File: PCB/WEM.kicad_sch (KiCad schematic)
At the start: 79 parts, among them J1 USB_C_Receptacle_USB2.0_14P, J2 MCU flashing pins, J3 Extensions' connectors, J4 Battery, J5 Reset, J6 Battery jumper, SW1 Kailh Mouse Scroll Wheel Enco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, SW2 LMB, SW3 MMB, SW4 RMB, SW5 FORWARD, SW6 BACK, SW7 SMMB, SW8 ON/OFF, U1 nRF52840, U2 MCP73871-2CC, U3 PAW3395DM-T6QU, U4 MCP1801T-3302I_OT, U5 LT1761ES5-2-TRMPBF, X1 32MHz

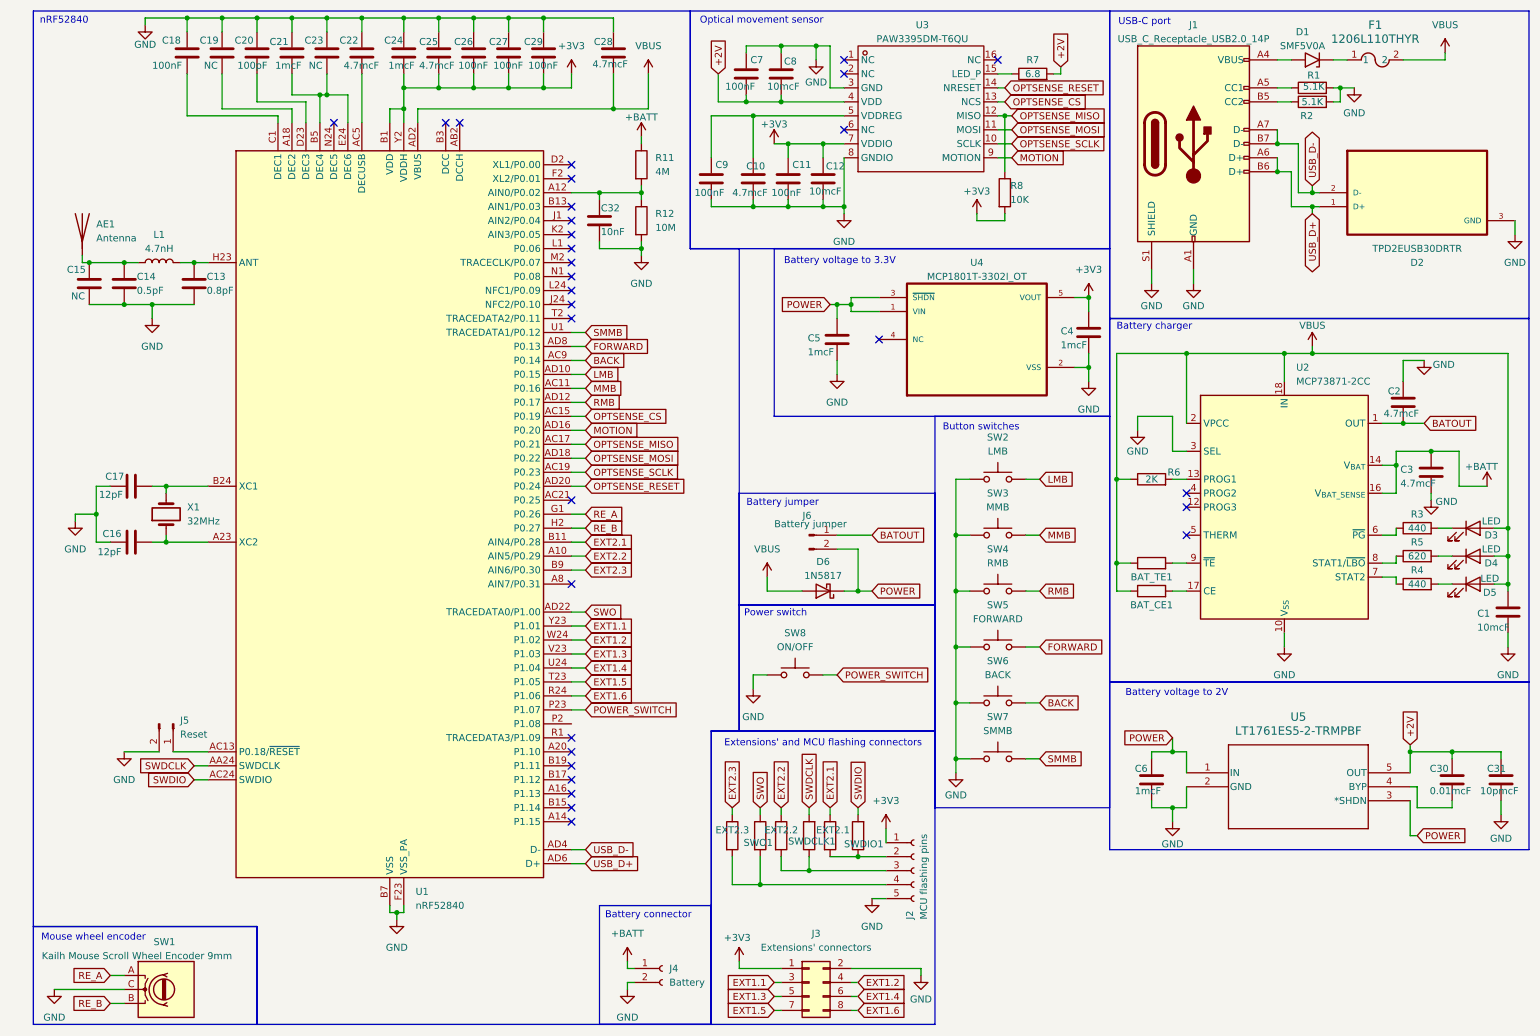
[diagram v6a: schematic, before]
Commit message: Started PCB routing
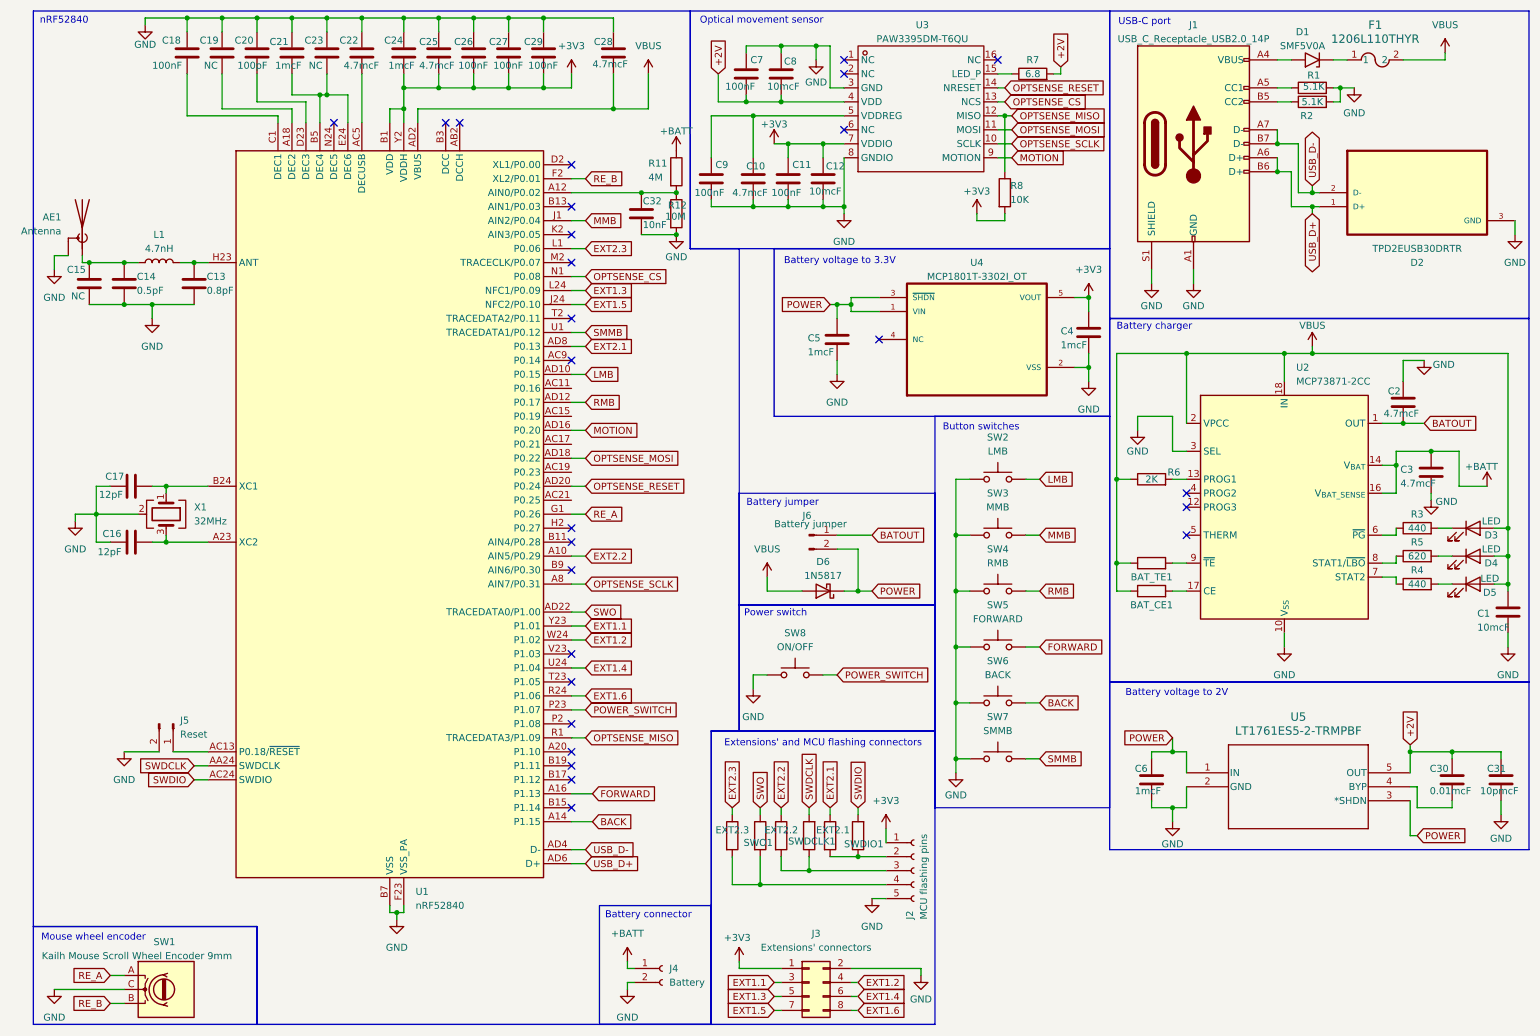
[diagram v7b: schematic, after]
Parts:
- removed X1: 32MHz, Crystal:Crystal_SMD_2016-4Pin_2.0x1.6mm, symbol Device:Crystal
- added X1: 32MHz, Crystal:Crystal_SMD_2016-4Pin_2.0x1.6mm, symbol Device:Crystal_GND24
- AE1: symbol Device:Antenna -> Device:Antenna_Shield
- C13, C14, C15, C16, C17, C18, C19, C20, C21, C22, C23, C24, C25, C26, C27, C28, C29: footprint Capacitor_SMD:C_0805_2012Metric_Pad1.18x1.45mm_HandSolder -> Capacitor_SMD:C_0603_1608Metric_Pad1.08x0.95mm_HandSolder
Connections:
- net BACK: now also U1.A14 (P1.15); no longer U1.AC9 (P0.14)
- net EXT1.3: now also U1.L24 (NFC1/P0.09); no longer U1.V23 (P1.03)
- net EXT1.5: now also U1.J24 (NFC2/P0.10); no longer U1.T23 (P1.05)
- net EXT2.1: now also U1.AD8 (P0.13); no longer U1.B11 (AIN4/P0.28)
- net EXT2.3: now also U1.L1 (P0.06); no longer U1.B9 (AIN6/P0.30)
- net FORWARD: now also U1.A16 (P1.13); no longer U1.AD8 (P0.13)
- net GND: now also AE1.2 (Shield), X1.2 (G), X1.4 (G)
- net MMB: now also U1.J1 (AIN2/P0.04); no longer U1.AC11 (P0.16)
- net OPTSENSE_CS: now also U1.N1 (P0.08); no longer U1.AC15 (P0.19)
- net OPTSENSE_MISO: now also U1.R1 (TRACEDATA3/P1.09); no longer U1.AC17 (P0.21)
- net OPTSENSE_SCLK: now also U1.A8 (AIN7/P0.31); no longer U1.AC19 (P0.23)
- net RE_B: now also U1.F2 (XL2/P0.01); no longer U1.H2 (P0.27)
- net at C16.2, U1.A23 (XC2): now also X1.3
- net at C17.2, U1.B24 (XC1): now also X1.1
- no-connect marks 31 -> 27
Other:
- moved on the sheet: C32, R11, R12

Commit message: Continued routing. It's hopeless
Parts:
- removed J5: Reset, Connector_PinHeader_2.54mm:PinHeader_1x02_P2.54mm_Vertical, symbol Connector:Conn_01x02_Pin
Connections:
- no-connect marks 27 -> 28
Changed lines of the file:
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@@
 	)
 	(no_connect
+		(at 44.45 147.32)
+	)
+	(no_connect
 		(at 110.49 149.86)
 	)
@@
 	(wire
 		(pts
-			(xy 38.1 147.32) (xy 44.45 147.32)
-		)
-		(stroke
-			(width 0)
-			(type default)
-		)
-	)
-	(wire
-		(pts
 			(xy 110.49 111.76) (xy 113.03 111.76)
 		)
@@
 	(wire
 		(pts
-			(xy 29.21 147.32) (xy 35.56 147.32)
-		)
-		(stroke
-			(width 0)
-			(type default)
-		)
-	)
-	(wire
-		(pts
 			(xy 250.19 26.67) (xy 252.73 26.67)
 		)
@@
 	)
 	(symbol
-		(lib_id "Connector:Conn_01x02_Pin")
-		(at 38.1 142.24 270)
-		(unit 1)
-		(exclude_from_sim no)
-		(in_bom yes)
-		(on_board yes)
-		(dnp no)
-		(fields_autoplaced yes)
-		(property "Reference" "J5"
-			(at 39.37 141.6049 90)
-			(effects
-				(font
-					(size 1.27 1.27)
-				)
-				(justify left)
-			)
-		)
-		(property "Value" "Reset"
-			(at 39.37 144.1449 90)
-			(effects
-				(font
-					(size 1.27 1.27)
-				)
-				(justify left)
-			)
-		)
-		(property "Footprint" "Connector_PinHeader_2.54mm:PinHeader_1x02_P2.54mm_Vertical"
-			(at 38.1 142.24 0)
-			(effects
-				(font
-					(size 1.27 1.27)
-				)
-				(hide yes)
-			)
-		)
-		(property "Datasheet" "~"
-			(at 38.1 142.24 0)
-			(effects
-				(font
-					(size 1.27 1.27)
-				)
-				(hide yes)
-			)
-		)
-		(property "Description" "Short to reset"
-			(at 38.1 142.24 0)
-			(effects
-				(font
-					(size 1.27 1.27)
-				)
-				(hide yes)
-			)
-		)
-		(pin "1"
-		)
-		(pin "2"
-		)
-		(instances
-			(project ""
-				(path "/4cb305f5-d3ed-4167-ba2e-2eb88ee18bc1"
-					(reference "J5")
-					(unit 1)
-				)
-			)
-		)
-	)
-	(symbol
 		(lib_id "Device:R")
 		(at 264.16 116.84 90)
@@
 					(unit 1)
 				)
-			)
-		)
-	)
-	(symbol
-		(lib_id "power:GND")
-		(at 29.21 147.32 0)
-		(unit 1)
-		(exclude_from_sim no)
-		(in_bom yes)
-		(on_board yes)
-		(dnp no)
-		(fields_autoplaced yes)
-		(property "Reference" "#PWR035"
-			(at 29.21 153.67 0)
-			(effects
-				(font
-					(size 1.27 1.27)
-				)
-				(hide yes)
-			)
-		)
-		(property "Value" "GND"
-			(at 29.21 152.4 0)
-			(effects
-				(font
-					(size 1.27 1.27)
-				)
-			)
-		)
-		(property "Footprint" ""
-			(at 29.21 147.32 0)
-			(effects
-				(font
-					(size 1.27 1.27)
-				)
-				(hide yes)
-			)
-		)
-		(property "Datasheet" ""
-			(at 29.21 147.32 0)
-			(effects
-				(font
-					(size 1.27 1.27)
-				)
-				(hide yes)
-			)
-		)
-		(property "Description" "Power symbol creates a global label with name \"GND\" , ground"
-			(at 29.21 147.32 0)
-			(effects
-				(font
-					(size 1.27 1.27)
-				)
-				(hide yes)
-			)
-		)
-		(pin "1"
-		)
-		(instances
-			(project ""
-				(path "/4cb305f5-d3ed-4167-ba2e-2eb88ee18bc1"
-					(reference "#PWR035")
-					(unit 1)
-				)
